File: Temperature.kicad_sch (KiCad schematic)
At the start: 29 parts, among them J3 Conn_01x24_Female, U8 LM321, U9 ADS7953SBDBT

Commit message: layed out adc components, abt 75% done probably?
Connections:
- net +3.3V: no longer U9.36 (VBD+)
- net GND: no longer U9.35 (BDGND)
- net GNDA: no longer U9.20 (AGND), U9.30 (AGND)
- net SPI_CLK: no longer U9.32 (SCLK)
- net SPI_CS: no longer U9.31 (*CS)
- net SPI_MISO: no longer U9.34 (SDO)
- net SPI_MOSI: no longer U9.33 (SDI)
- net VDDA: no longer U9.29 (VA+)
- net temp1: no longer U9.28 (CH0)
- net temp2: no longer U9.27 (CH1)
- net temp3: no longer U9.26 (CH2)
- net temp4: no longer U9.25 (CH3)
- net temp5: no longer U9.24 (CH4)
- net temp6: no longer U9.23 (CH5)
- net temp7: no longer U9.22 (CH6)
- net temp8: no longer U9.21 (CH7)
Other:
- moved on the sheet: U9
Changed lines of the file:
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@@
     )
   )
-  (symbol (lib_id "utsvt-chips:ADS7953SBDBT") (at 237.49 31.75 0) (mirror y) (unit 1)
-    (in_bom yes) (on_board yes) (dnp no) (fields_autoplaced)
-    (property "Reference" "U9" (at 204.47 21.59 0)
+  (symbol (lib_id "utsvt-chips:ADS7953SBDBT") (at 237.49 31.75 0) (unit 1)
+    (in_bom yes) (on_board yes) (dnp no)
+    (property "Reference" "U9" (at 270.51 21.59 0)
       (effects (font (size 1.524 1.524)))
     )
-    (property "Value" "ADS7953SBDBT" (at 204.47 24.13 0)
+    (property "Value" "ADS7953SBDBT" (at 270.51 24.13 0)
       (effects (font (size 1.524 1.524)))
     )

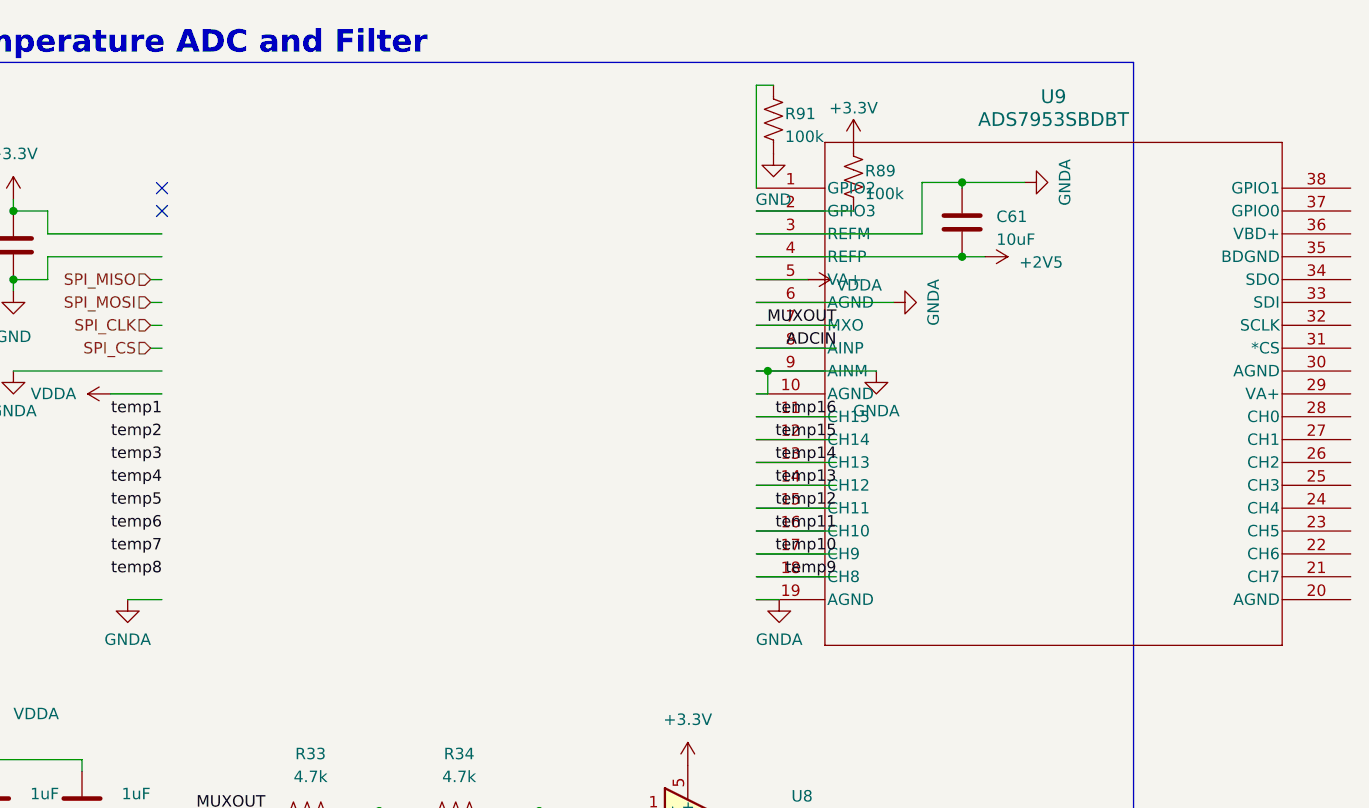
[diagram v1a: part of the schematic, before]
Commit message: Revert "layed out adc components, abt 75% done probably?"
This reverts commit 5305dcecdd1d1d4d875daf20a76a2afe21639337.
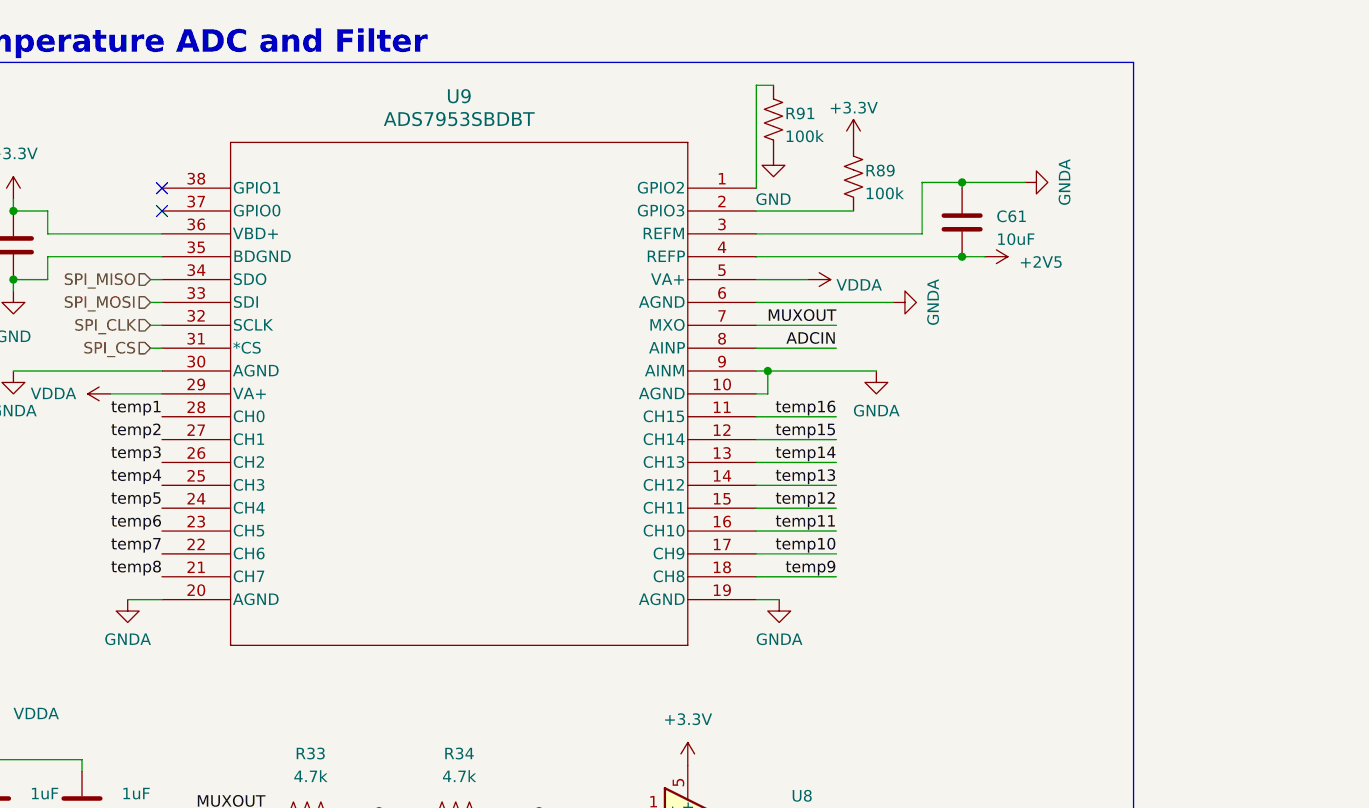
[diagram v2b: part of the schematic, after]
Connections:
- net +3.3V: now also U9.36 (VBD+)
- net GND: now also U9.35 (BDGND)
- net GNDA: now also U9.20 (AGND), U9.30 (AGND)
- net SPI_CLK: now also U9.32 (SCLK)
- net SPI_CS: now also U9.31 (*CS)
- net SPI_MISO: now also U9.34 (SDO)
- net SPI_MOSI: now also U9.33 (SDI)
- net VDDA: now also U9.29 (VA+)
- net temp1: now also U9.28 (CH0)
- net temp2: now also U9.27 (CH1)
- net temp3: now also U9.26 (CH2)
- net temp4: now also U9.25 (CH3)
- net temp5: now also U9.24 (CH4)
- net temp6: now also U9.23 (CH5)
- net temp7: now also U9.22 (CH6)
- net temp8: now also U9.21 (CH7)
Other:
- moved on the sheet: U9
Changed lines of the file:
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@@
     )
   )
-  (symbol (lib_id "utsvt-chips:ADS7953SBDBT") (at 237.49 31.75 0) (unit 1)
-    (in_bom yes) (on_board yes) (dnp no)
-    (property "Reference" "U9" (at 270.51 21.59 0)
+  (symbol (lib_id "utsvt-chips:ADS7953SBDBT") (at 237.49 31.75 0) (mirror y) (unit 1)
+    (in_bom yes) (on_board yes) (dnp no) (fields_autoplaced)
+    (property "Reference" "U9" (at 204.47 21.59 0)
       (effects (font (size 1.524 1.524)))
     )
-    (property "Value" "ADS7953SBDBT" (at 270.51 24.13 0)
+    (property "Value" "ADS7953SBDBT" (at 204.47 24.13 0)
       (effects (font (size 1.524 1.524)))
     )
